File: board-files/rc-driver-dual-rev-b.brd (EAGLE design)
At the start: 29.6 x 17.5 mm, 20 parts

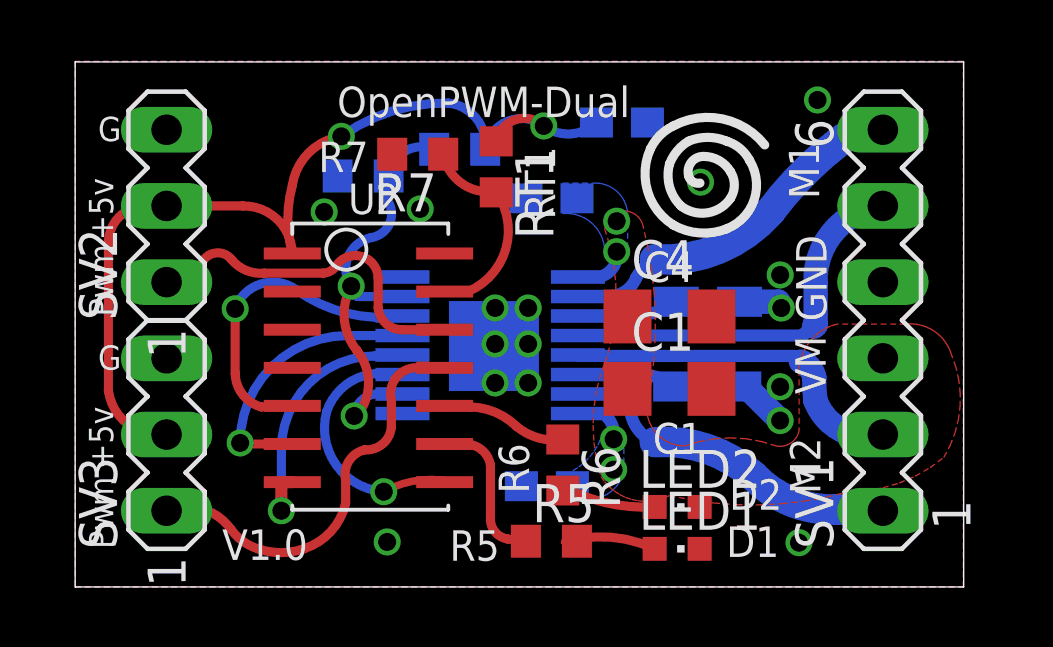
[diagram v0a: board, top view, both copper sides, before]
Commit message: First pass layout of revB designed that include 5V regulator Improved part outlines in library.
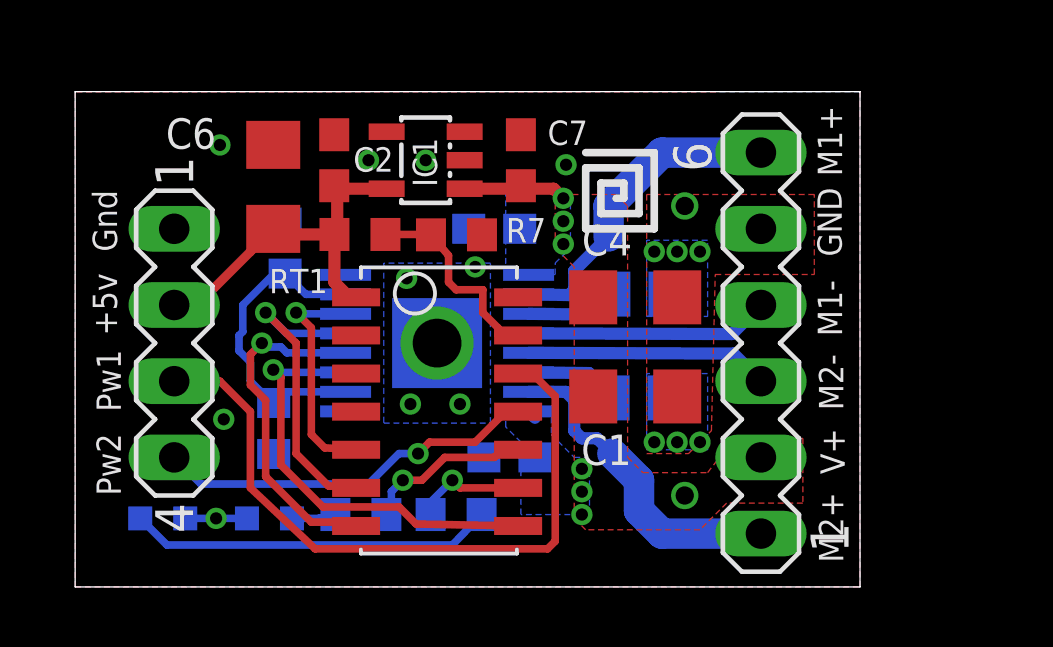
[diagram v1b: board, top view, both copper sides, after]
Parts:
- removed LED1: GREEN, led:CHIPLED_0603
- removed LED2: RED, led:CHIPLED_0603
- removed SV2, SV3: (no value), con-lstb:MA03-1
- added C6: 10uF, resistor:C1206
- added C7: 1uF, resistor:C0603
- added D1: GREEN, led:CHIPLED_0603
- added D2: RED, led:CHIPLED_0603
- added IC1: (no value), v-reg-micrel:SOT23-5
- added SV4: (no value), con-lstb:MA04-1
- C1, C4: value 10uf -> 10uF
- C2, C3, C5: value 0.1uf -> 1uF
- R1, R2: device resistor:R0805W -> resistor:R0805
- R3: value 5600 -> 5.6k
- R4: value 1300 -> 1.3k
- R7: value (none) -> 5.6k
- RT1: value (none) -> 10k
- moved C2 9.67 mm to (8.64, 14.2), flipped to the top, turned to 90 degrees
- moved R4 8.93 mm to (6.62, 5.28), turned to 270 degrees
- moved R6 6.93 mm to (9.53, 2.41), flipped to the bottom, turned to 0 degrees
- moved R3 6.69 mm to (7.00, 11.3), turned to 270 degrees
- moved RT1 5.07 mm to (9.49, 11.7), turned to 0 degrees
- moved SV1 4.13 mm to (22.9, 8.13)
- moved U$1 3.56 mm to (12.1, 5.84)
- moved R5 3.30 mm to (12.7, 2.41), flipped to the bottom, turned to 180 degrees
- moved R7 2.98 mm to (12.7, 11.7), turned to 0 degrees
- moved R1 2.32 mm to (18.8, 6.30)
- moved R2 2.30 mm to (18.8, 9.76)
- moved C5 2.16 mm to (14.0, 11.9)
- moved U$2 2.10 mm to (12.1, 8.13)
- moved C3 1.57 mm to (14.5, 4.32)
- moved C4 1.31 mm to (18.7, 9.65)
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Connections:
- net LED renamed LED1
- removed net VM: C1.1, C3.1, C4.1, C5.1, SV1.3, U$2.P$16, U$2.P$9
- new net +12V: C1.1, C3.1, C4.1, C5.1, C7.1, IC1.1, SV1.2, U$2.P$16, U$2.P$9
- net +5V: now also C6.1, IC1.5, SV4.2; no longer SV2.2, SV3.2
- net GND: now also C6.2, C7.2, D1.C, D2.C, IC1.2, SV1.5, SV4.1; no longer LED1.C, LED2.C, SV1.4, SV2.3, SV3.3
- net MOTOR1-2: now also SV1.4; no longer SV1.5
- net MOTOR2-1: now also SV1.3; no longer SV1.2
- net N$3: now also D2.A; no longer LED2.A
- net N$4: now also D1.A; no longer LED1.A
- net PWM1: now also SV4.3; no longer SV2.1
- net PWM2: now also SV4.4; no longer SV3.1
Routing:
- net +5V: track 30.5 -> 17.2 mm, vias 2 -> 0
- net PWM1: track 11.0 -> 23.0 mm
- net N$4: track 3.35 -> 12.2 mm
- net OUTPUT3: track 8.45 -> 14.4 mm
- net MOTOR1-2: track 12.9 -> 8.15 mm
- net +12V: track 0.00 -> 3.86 mm, vias 0 -> 7
- net MOTOR2-1: track 11.6 -> 8.13 mm
- net VM: track 3.50 -> 0.00 mm, vias 4 -> 0
- net VREF: track 14.2 -> 10.9 mm, vias 2 -> 0
- net OUTPUT4: track 8.70 -> 11.5 mm
- net OUTPUT1: track 10.4 -> 7.78 mm
- net OUTPUT2: track 8.65 -> 10.5 mm
- net N$3: track 3.11 -> 1.46 mm
- net LED2: track 4.14 -> 5.73 mm, vias 0 -> 1
- net MOTOR1-1: track 12.0 -> 10.7 mm
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- added copper zone on layer 1, net +12V
- added copper zone on layer 16, net +12V
- removed copper zone on layer 1, net VM
- removed copper zone on layer 16, net VM
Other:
- board size 29.6 x 17.5 mm -> 26.2 x 16.5 mm
- board text added: "Gnd"
- board text added: "M1+"
- board text added: "M1-"
- board text added: "M2+"
- board text added: "M2-"
- board text added: "OpenPWM-Dual RevB"
- board text added: "Pw1"
- board text added: "Pw2"
- board text added: "V+"
- board text removed: "C1"
- board text removed: "C2"
- board text removed: "C3"
- board text removed: "C4"
- board text removed: "C5"
- board text removed: "D1"
- board text removed: "D2"
- board text removed: "G"
- board text removed: "M1"
- board text removed: "M2"
- board text removed: "OpenPWM-Dual"
- board text removed: "Pwm"
- board text removed: "R1"
- board text removed: "R2"
- board text removed: "R3"
- board text removed: "R4"
- board text removed: "R5"
- board text removed: "R6"
- board text removed: "R7"
- board text removed: "RT1"
- board text removed: "U2"
- board text removed: "V1.0"
- board text removed: "VM"

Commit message: Added optional 6-DOF IMU to circuit board. Changed some parts to 0402.
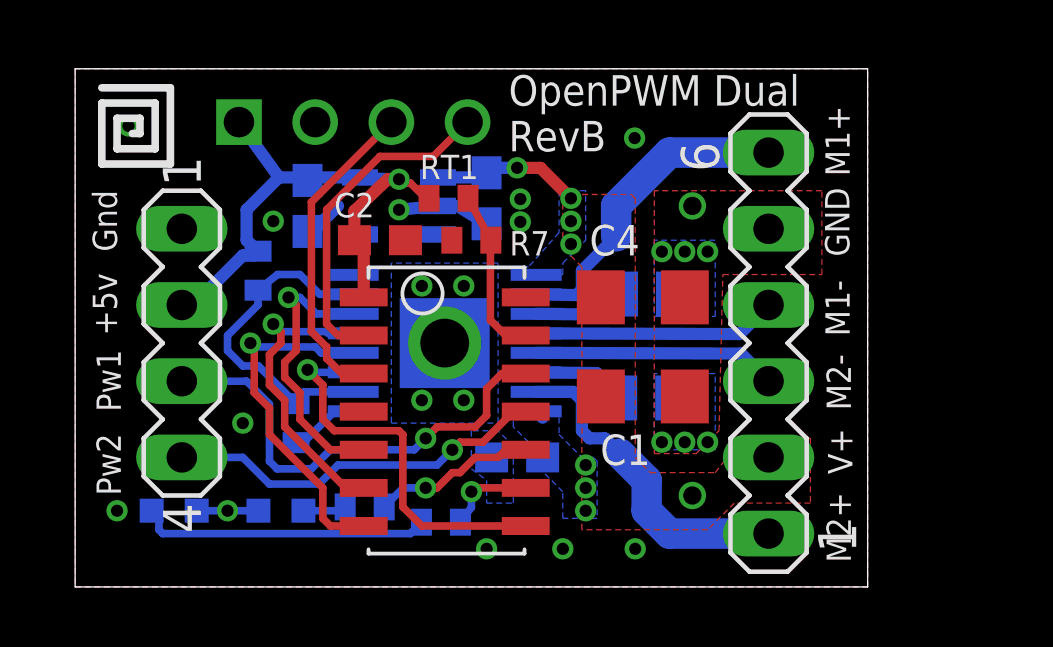
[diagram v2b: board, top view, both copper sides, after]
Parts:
- removed C7: 1uF, resistor:C0603
- added U1: MPU6050-NO-INT, rc-parts:MPU6050-NO-INT
- C2: value 1uF -> 2.2uF
- C6: value 10uF -> 2.2uF; device resistor:C1206 -> resistor:C0603
- R3, R4, R5, R6, R7, RT1: device resistor:R0603 -> resistor:R0402
- moved RT1 3.19 mm to (12.4, 13.0)
- moved C2 3.07 mm to (10.2, 11.6), turned to 0 degrees
- moved IC1 1.76 mm to (10.8, 12.7), flipped to the bottom, turned to 270 degrees
- moved C6 1.31 mm to (7.75, 12.7), flipped to the bottom, turned to 270 degrees
- moved R3 1.18 mm to (6.10, 10.5)
- moved C5 1.05 mm to (13.7, 13.0), turned to 270 degrees
- moved R4 0.77 mm to (7.37, 5.46)
- moved R5 0.57 mm to (12.2, 2.16), turned to 0 degrees
- moved R7 0.53 mm to (13.2, 11.6), turned to 180 degrees
- moved D1 0.46 mm to (3.30, 2.54)
- moved D2 0.46 mm to (6.86, 2.54)
- moved R6 0.28 mm to (9.65, 2.67)
- moved R1 0.25 mm to (19.0, 6.30)
- moved SV1 0.25 mm to (23.1, 8.13)
- moved U$1 0.25 mm to (12.3, 5.84)
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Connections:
- new net SCL: U$1.P$2, U1.4
- new net SDA: U$1.P$3, U1.3
- net +12V: no longer C7.1
- net +5V: now also U1.1
- net GND: now also U1.2; no longer C7.2
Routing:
- net SCL: track 0.00 -> 11.1 mm
- net SDA: track 0.00 -> 10.6 mm
- net PWM1: track 23.0 -> 15.6 mm, vias 0 -> 1
- net GND: track 2.10 -> 8.89 mm, vias 18 -> 24
- net N$4: track 12.2 -> 9.70 mm
- net +5V: track 17.2 -> 19.3 mm, vias 0 -> 1
- net OUTPUT1: track 7.78 -> 9.47 mm
- net +12V: track 3.86 -> 5.47 mm, vias 7 -> 8
- net OUTPUT3: track 14.4 -> 13.1 mm
- net T-OUT: track 6.97 -> 5.68 mm
- net LED1: track 3.74 -> 3.00 mm
- net VREF: track 10.9 -> 11.6 mm
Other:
- board size 26.2 x 16.5 mm -> 26.4 x 17.3 mm
- board text added: "OpenPWM Dual"
- board text added: "RevB"
- board text removed: "OpenPWM-Dual RevB"
